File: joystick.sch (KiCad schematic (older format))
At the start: 5 parts

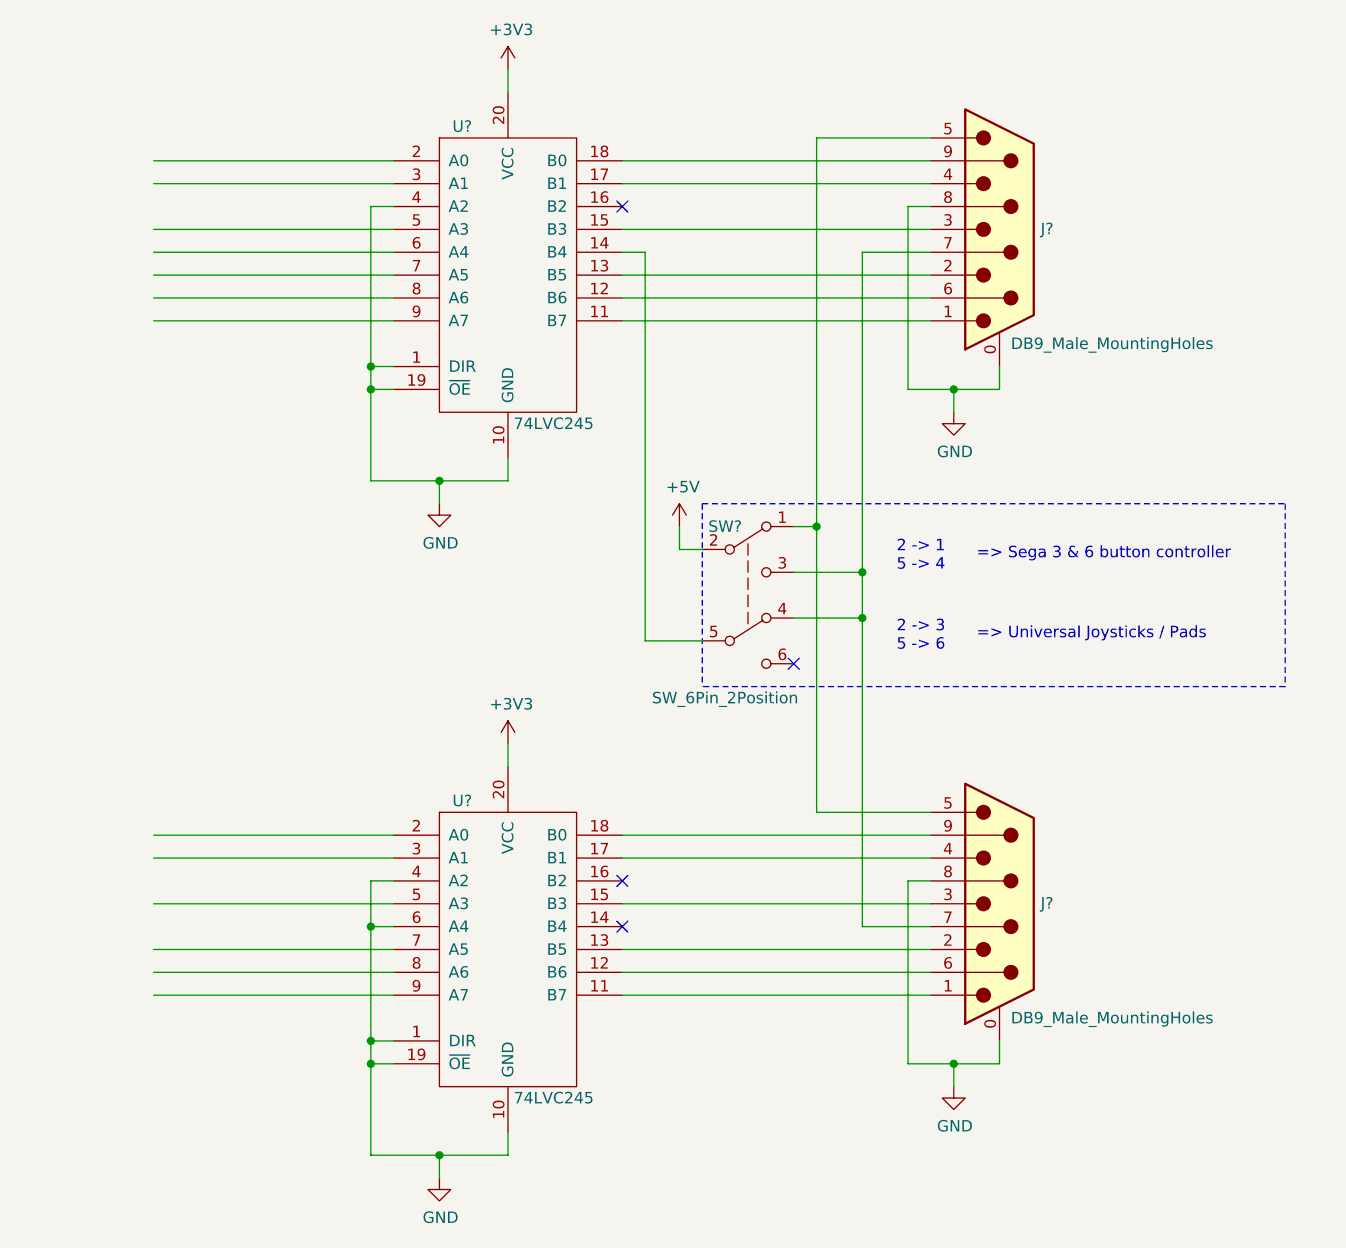
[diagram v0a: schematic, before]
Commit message: Joystick net assigned.
Signed-off-by: Kali Prasad <kprasadvnsi@protonmail.com>
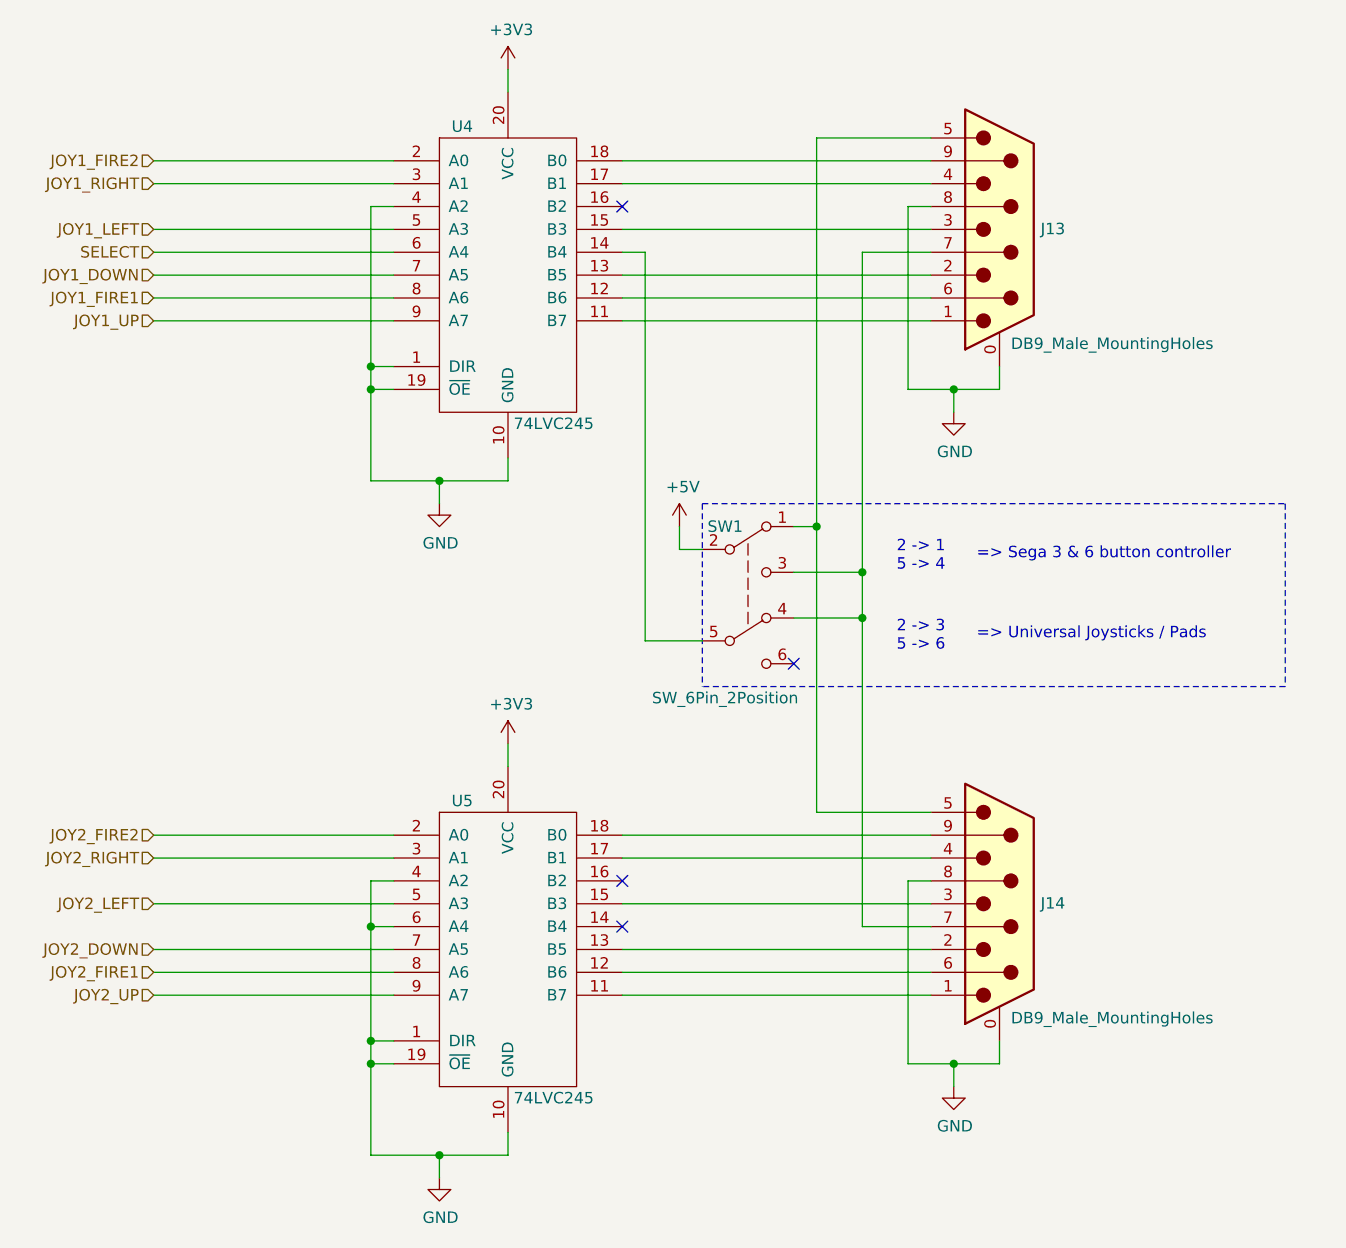
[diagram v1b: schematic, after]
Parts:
- gave numbers to parts that had none: 5
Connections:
- net labels added: JOY1_DOWN, JOY1_FIRE1, JOY1_FIRE2, JOY1_LEFT, JOY1_RIGHT, JOY1_UP, JOY2_DOWN, JOY2_FIRE1, JOY2_FIRE2, JOY2_LEFT, JOY2_RIGHT, JOY2_UP, SELECT
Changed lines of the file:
@@
 $EndDescr
 $Comp
-L Connector:DB9_Male_MountingHoles J?
+L Connector:DB9_Male_MountingHoles J13
 U 1 1 5D1888BF
 P 7200 1950
-F 0 "J?" H 7380 1952 50  0000 L CNN
+F 0 "J13" H 7380 1952 50  0000 L CNN
 F 1 "DB9_Male_MountingHoles" H 7250 1450 50  0000 L CNN
 F 2 "" H 7200 1950 50  0001 C CNN
@@
 $EndComp
 $Comp
-L lt_eval_board:74LVC245 U?
+L lt_eval_board:74LVC245 U4
 U 1 1 5D1C50F6
 P 5050 2150
-F 0 "U?" H 4850 2800 50  0000 C CNN
+F 0 "U4" H 4850 2800 50  0000 C CNN
 F 1 "74LVC245" H 5250 1500 50  0000 C CNN
 F 2 "" H 5050 2150 60  0000 C CNN
@@
 $EndComp
 $Comp
-L power:GND #PWR?
+L power:GND #PWR054
 U 1 1 5D1C6E73
 P 7000 2750
-F 0 "#PWR?" H 7000 2500 50  0001 C CNN
+F 0 "#PWR054" H 7000 2500 50  0001 C CNN
 F 1 "GND" H 7005 2577 50  0000 C CNN
 F 2 "" H 7000 2750 50  0001 C CNN
@@
 	4450 2650 4450 2550
 $Comp
-L power:GND #PWR?
+L power:GND #PWR049
 U 1 1 5D1D0680
 P 4750 3150
-F 0 "#PWR?" H 4750 2900 50  0001 C CNN
+F 0 "#PWR049" H 4750 2900 50  0001 C CNN
 F 1 "GND" H 4755 2977 50  0000 C CNN
 F 2 "" H 4750 3150 50  0001 C CNN
@@
 NoConn ~ 5550 1850
 $Comp
-L lt_eval_board:SW_6Pin_2Position SW?
+L lt_eval_board:SW_6Pin_2Position SW1
 U 1 1 5D1E2DAD
 P 6100 3550
-F 0 "SW?" H 6000 3850 50  0000 C CNN
+F 0 "SW1" H 6000 3850 50  0000 C CNN
 F 1 "SW_6Pin_2Position" H 6000 3100 50  0000 C CNN
 F 2 "" H 6100 3750 50  0001 C CNN
@@
 	5550 2050 5650 2050
 $Comp
-L power:+5V #PWR?
+L power:+5V #PWR053
 U 1 1 5D1E86CD
 P 5800 3250
-F 0 "#PWR?" H 5800 3100 50  0001 C CNN
+F 0 "#PWR053" H 5800 3100 50  0001 C CNN
 F 1 "+5V" H 5815 3423 50  0000 C CNN
 F 2 "" H 5800 3250 50  0001 C CNN
@@
 	5050 1250 5050 1350
 $Comp
-L power:+3V3 #PWR?
+L power:+3V3 #PWR051
 U 1 1 5D202630
 P 5050 1250
-F 0 "#PWR?" H 5050 1100 50  0001 C CNN
+F 0 "#PWR051" H 5050 1100 50  0001 C CNN
 F 1 "+3V3" H 5065 1423 50  0000 C CNN
 F 2 "" H 5050 1250 50  0001 C CNN
@@
 $EndComp
 $Comp
-L Connector:DB9_Male_MountingHoles J?
+L Connector:DB9_Male_MountingHoles J14
 U 1 1 5D20637F
 P 7200 4900
-F 0 "J?" H 7380 4902 50  0000 L CNN
+F 0 "J14" H 7380 4902 50  0000 L CNN
 F 1 "DB9_Male_MountingHoles" H 7250 4400 50  0000 L CNN
 F 2 "" H 7200 4900 50  0001 C CNN
@@
 $EndComp
 $Comp
-L lt_eval_board:74LVC245 U?
+L lt_eval_board:74LVC245 U5
 U 1 1 5D206389
 P 5050 5100
-F 0 "U?" H 4850 5750 50  0000 C CNN
+F 0 "U5" H 4850 5750 50  0000 C CNN
 F 1 "74LVC245" H 5250 4450 50  0000 C CNN
 F 2 "" H 5050 5100 60  0000 C CNN
@@
 $EndComp
 $Comp
-L power:GND #PWR?
+L power:GND #PWR055
 U 1 1 5D206393
 P 7000 5700
-F 0 "#PWR?" H 7000 5450 50  0001 C CNN
+F 0 "#PWR055" H 7000 5450 50  0001 C CNN
 F 1 "GND" H 7005 5527 50  0000 C CNN
 F 2 "" H 7000 5700 50  0001 C CNN
@@
 	4450 5600 4450 5500
 $Comp
-L power:GND #PWR?
+L power:GND #PWR050
 U 1 1 5D2063B1
 P 4750 6100
-F 0 "#PWR?" H 4750 5850 50  0001 C CNN
+F 0 "#PWR050" H 4750 5850 50  0001 C CNN
 F 1 "GND" H 4755 5927 50  0000 C CNN
 F 2 "" H 4750 6100 50  0001 C CNN
@@
 	5050 4200 5050 4300
 $Comp
-L power:+3V3 #PWR?
+L power:+3V3 #PWR052
 U 1 1 5D2063C6
 P 5050 4200
-F 0 "#PWR?" H 5050 4050 50  0001 C CNN
+F 0 "#PWR052" H 5050 4050 50  0001 C CNN
 F 1 "+3V3" H 5065 4373 50  0000 C CNN
 F 2 "" H 5050 4200 50  0001 C CNN
@@
 Text Notes 7100 3750 0    50   ~ 0
 => Universal Joysticks / Pads
+Text HLabel 3500 2350 0    50   Input ~ 0
+JOY1_UP
+Text HLabel 3500 2150 0    50   Input ~ 0
+JOY1_DOWN
+Text HLabel 3500 1950 0    50   Input ~ 0
+JOY1_LEFT
+Text HLabel 3500 1750 0    50   Input ~ 0
+JOY1_RIGHT
+Text HLabel 3500 2250 0    50   Input ~ 0
+JOY1_FIRE1
+Text HLabel 3500 1650 0    50   Input ~ 0
+JOY1_FIRE2
+Text HLabel 3500 2050 0    50   Input ~ 0
+SELECT
+Text HLabel 3500 5300 0    50   Input ~ 0
+JOY2_UP
+Text HLabel 3500 5100 0    50   Input ~ 0
+JOY2_DOWN
+Text HLabel 3500 4900 0    50   Input ~ 0
+JOY2_LEFT
+Text HLabel 3500 4700 0    50   Input ~ 0
+JOY2_RIGHT
+Text HLabel 3500 5200 0    50   Input ~ 0
+JOY2_FIRE1
+Text HLabel 3500 4600 0    50   Input ~ 0
+JOY2_FIRE2
 $EndSCHEMATC
